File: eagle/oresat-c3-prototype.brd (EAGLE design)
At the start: 99.8 x 94.7 mm, 98 parts, among them J1 J-SAMTEC-TFM-110-X1-XXX-D-RA, J2 U.FL, J3 U.FL, J4 U.FL, J6 J-SAMTEC-TFM-120-X1-XXX-D-RA, J7 FTSH-105-XX-X-DV-K, J8 SD_CARD_SOCKET, Q1 MOSFET-PCH-SOT23-6, Q3 MOSFET-PCH-SOT23-6, Q4 MOSFET-PCH-SOT23-6, Q5 PMV45EN, Q6 PMV45EN, U2 TCAN330, U3 TCAN330, U4 MAX4211CETE, U5 TPS62111RSA, U6 MAX6373KA+21-0078H-L, X1 16MHZ-2.5x2mm

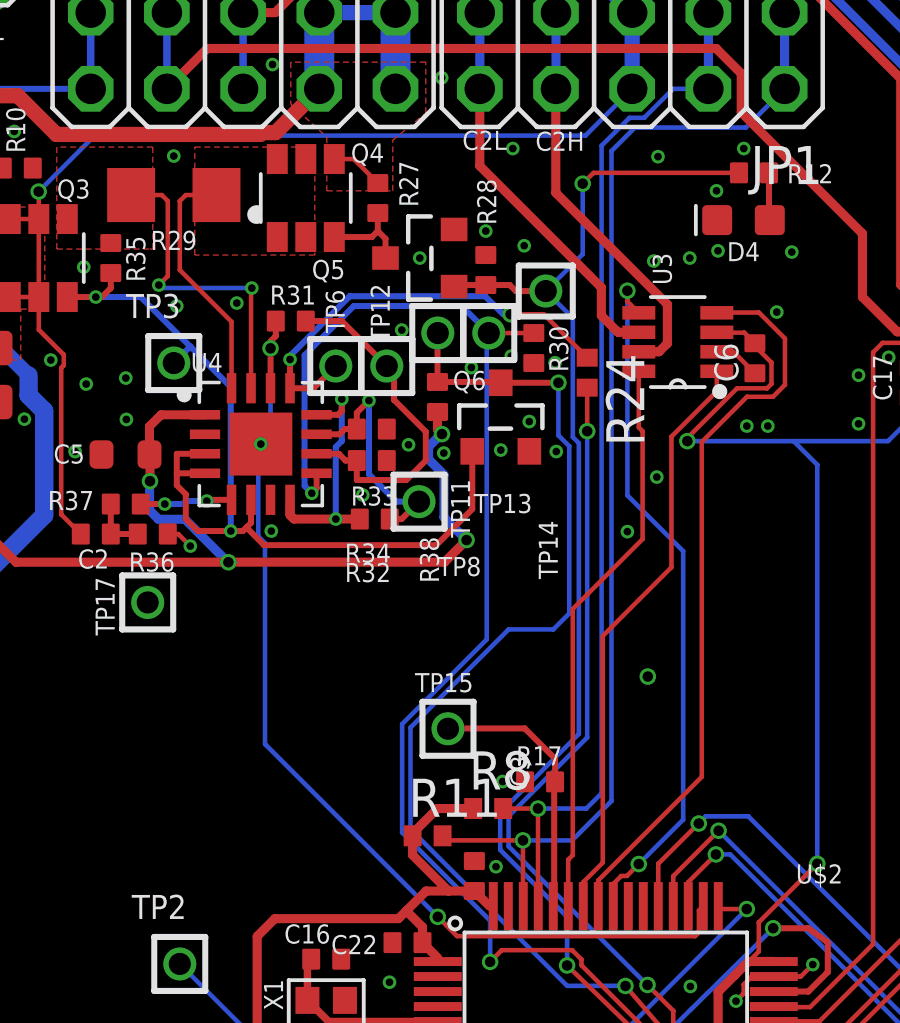
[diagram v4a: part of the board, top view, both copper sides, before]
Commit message: Fixed a couple other error check items
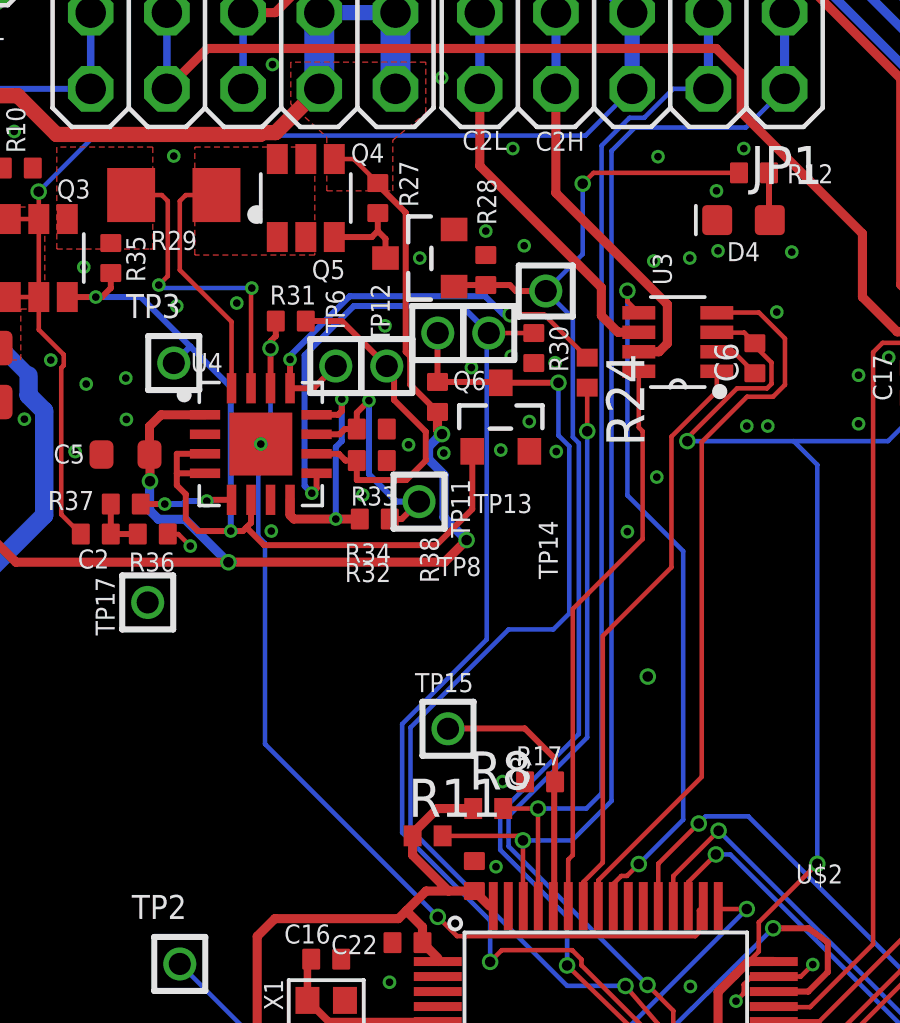
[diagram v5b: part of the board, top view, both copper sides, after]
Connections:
- removed net N$385: Q4.4, R27.2
- net 3.3V: now also Q4.4, R27.2
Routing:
- net 3.3V: track 214.9 -> 225.2 mm
- net N$385: track 1.78 -> 0.00 mm
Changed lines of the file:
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@@
 <wire x1="37.78" y1="43.28" x2="37.78" y2="45.72" width="0.1524" layer="1"/>
 <wire x1="37.525" y1="43.025" x2="37.78" y2="43.28" width="0.1524" layer="1"/>
+<contactref element="R27" pad="2"/>
+<contactref element="Q4" pad="4"/>
+<wire x1="46.4" y1="75.6" x2="45.6" y2="76.4" width="0.1524" layer="1"/>
+<wire x1="45.6" y1="76.4" x2="44.95" y2="76.4" width="0.1524" layer="1"/>
+<wire x1="47.48105" y1="69.823525" x2="47.3301" y2="69.974475" width="0.2032" layer="1"/>
+<wire x1="48.39" y1="67.97" x2="47.48105" y2="68.87895" width="0.2032" layer="1"/>
+<wire x1="46.4" y1="75.5434125" x2="46.4" y2="75.6" width="0.2032" layer="1"/>
+<wire x1="47.48105" y1="68.87895" x2="47.48105" y2="69.823525" width="0.2032" layer="1"/>
+<wire x1="47.3301" y1="69.974475" x2="47.3301" y2="74.6133125" width="0.2032" layer="1"/>
+<wire x1="47.3301" y1="74.6133125" x2="46.4" y2="75.5434125" width="0.2032" layer="1"/>
 </signal>
 <signal name="SDAOPT2">
@@
 <via x="50" y="74" extent="1-16" drill="0.254"/>
 <via x="52.31" y="69.61" extent="1-16" drill="0.254"/>
-<via x="47.2" y="70.7" extent="1-16" drill="0.254"/>
+<via x="46.64" y="70.84" extent="1-16" drill="0.254"/>
 <via x="34.28" y="77.32" extent="1-16" drill="0.254"/>
 <wire x1="31.575" y1="69.125" x2="32.275" y2="69.125" width="0.3" layer="1"/>
@@
 <contactref element="U$3" pad="1"/>
 <contactref element="U$3" pad="THERMAL"/>
-<contactref element="C1" pad="1"/>
 <contactref element="R9" pad="1"/>
 <contactref element="R6" pad="1"/>
@@
 <contactref element="JP2" pad="9"/>
 <via x="55.4" y="59.15" extent="1-16" drill="0.35"/>
+<contactref element="C1" pad="1"/>
 </signal>
 <signal name="PA5/SPI1_SCK">
@@
 <wire x1="55.615" y1="85.625" x2="59.96" y2="81.28" width="0.3048" layer="16"/>
 <wire x1="59.96" y1="81.28" x2="59.96" y2="78.74" width="0.3048" layer="16"/>
-<contactref element="R11" pad="2"/>
-<wire x1="51.239025" y1="53.689025" x2="48.710975" y2="53.689025" width="0.1524" layer="1"/>
-<wire x1="48.710975" y1="53.689025" x2="48.56" y2="53.84" width="0.1524" layer="1"/>
 <wire x1="54.97" y1="77.45" x2="58.67" y2="77.45" width="0.1524" layer="16"/>
 <wire x1="58.67" y1="77.45" x2="59.96" y2="78.74" width="0.1524" layer="16"/>
 <wire x1="54.1902" y1="76.67" x2="54.97" y2="77.4498" width="0.1524" layer="16"/>
 <wire x1="54.97" y1="77.4498" x2="54.97" y2="77.45" width="0.1524" layer="16"/>
+<contactref element="R11" pad="2"/>
+<wire x1="51.239025" y1="53.689025" x2="51.089025" y2="53.839025" width="0.1524" layer="1"/>
+<wire x1="51.089025" y1="53.839025" x2="48.560975" y2="53.839025" width="0.1524" layer="1"/>
+<wire x1="48.560975" y1="53.839025" x2="48.56" y2="53.84" width="0.1524" layer="1"/>
 </signal>
 <signal name="SPARE1">
@@
 <vertex x="46.2" y="84.6"/>
 </polygon>
-<contactref element="R5" pad="2"/>
-<contactref element="C1" pad="2"/>
-<contactref element="U$3" pad="4"/>
 <wire x1="46.99" y1="81.28" x2="46.73" y2="81.54" width="0.508" layer="16"/>
 <wire x1="46.73" y1="88.624" x2="46.73" y2="81.54" width="0.508" layer="16"/>
@@
 <wire x1="42.991" y1="77.281" x2="42.5421875" y2="77.281" width="0.508" layer="1"/>
 <wire x1="42.5421875" y1="77.281" x2="42.4811875" y2="77.22" width="0.508" layer="1"/>
-<wire x1="34.400003125" y1="78.509996875" x2="25.00174375" y2="78.509996875" width="0.508" layer="1"/>
 <wire x1="42.4811875" y1="77.22" x2="35.69" y2="77.22" width="0.508" layer="1"/>
 <wire x1="35.69" y1="77.22" x2="34.400003125" y2="78.509996875" width="0.508" layer="1"/>
+<contactref element="R5" pad="2"/>
+<contactref element="C1" pad="2"/>
+<contactref element="U$3" pad="4"/>
 <wire x1="25.00174375" y1="78.509996875" x2="22.309996875" y2="78.509996875" width="0.508" layer="1"/>
 <wire x1="22.309996875" y1="78.509996875" x2="22.06" y2="78.26" width="0.508" layer="1"/>
 <wire x1="19.255" y1="78.235" x2="22.035" y2="78.235" width="0.5" layer="1"/>
 <wire x1="22.035" y1="78.235" x2="22.06" y2="78.26" width="0.5" layer="1"/>
+<wire x1="34.400003125" y1="78.509996875" x2="25.00174375" y2="78.509996875" width="0.508" layer="1"/>
 </signal>
 <signal name="SDAOPT5">
@@
 <wire x1="54.345" y1="84.355" x2="57.42" y2="81.28" width="0.3048" layer="16"/>
 <wire x1="57.42" y1="81.28" x2="57.42" y2="78.74" width="0.3048" layer="16"/>
-<contactref element="R8" pad="2"/>
-<wire x1="51.74" y1="54.75" x2="50.58" y2="54.75" width="0.1524" layer="1"/>
 <wire x1="54.79" y1="77.7748" x2="55.2798" y2="77.7748" width="0.1524" layer="16"/>
 <wire x1="56.245" y1="78.74" x2="57.42" y2="78.74" width="0.1524" layer="16"/>
@@
 <wire x1="51.74" y1="54.75" x2="53.35106875" y2="54.75" width="0.1524" layer="16"/>
 <wire x1="53.35106875" y1="54.75" x2="53.8608" y2="55.25973125" width="0.1524" layer="16"/>
+<contactref element="R8" pad="2"/>
+<wire x1="51.74" y1="54.75" x2="50.58" y2="54.75" width="0.1524" layer="1"/>
 </signal>
 <signal name="OPD_PWR">
@@
 <wire x1="58.155" y1="86.465" x2="70.3014" y2="74.3186" width="0.3048" layer="16"/>
 </signal>
-<signal name="N$385">
-<contactref element="R27" pad="2"/>
-<contactref element="Q4" pad="4"/>
-<wire x1="46.4" y1="75.6" x2="45.6" y2="76.4" width="0.1524" layer="1"/>
-<wire x1="45.6" y1="76.4" x2="44.95" y2="76.4" width="0.1524" layer="1"/>
-</signal>
 <signal name="N$400">

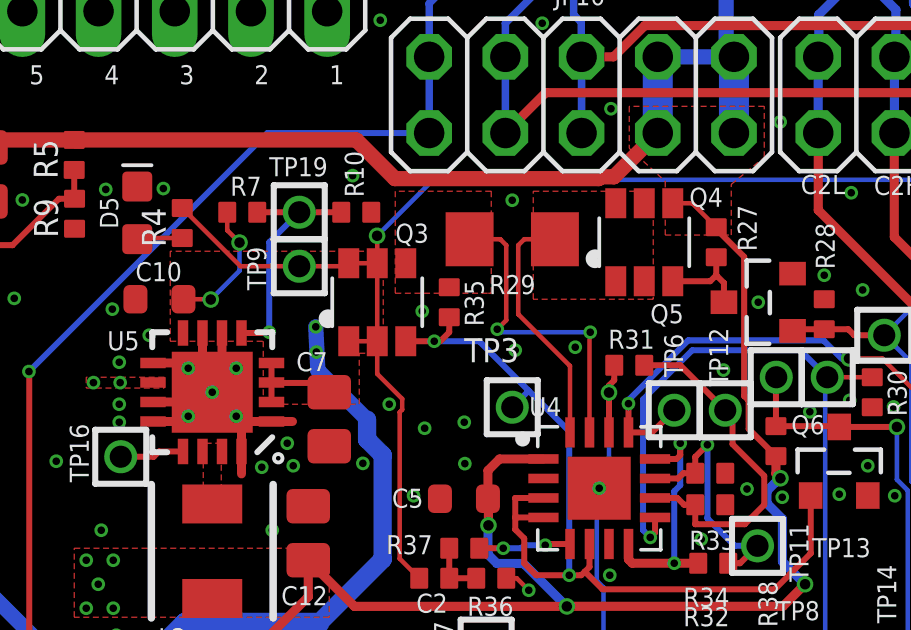
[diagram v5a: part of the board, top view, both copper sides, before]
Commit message: Fixed VBUSP routing around the SPS
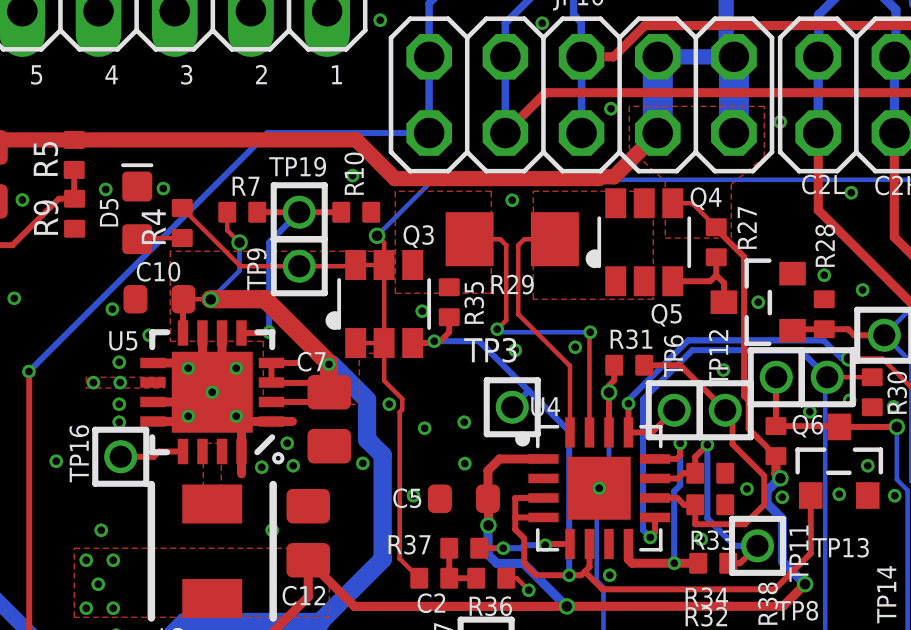
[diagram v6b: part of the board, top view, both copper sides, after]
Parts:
- moved Q3 0.24 mm to (35.3, 73.0)
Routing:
- net VBUSP: track 105.5 -> 112.8 mm, vias 5 -> 4
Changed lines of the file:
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@@
 <attribute name="VALUE" x="32.6" y="64.8" size="0.635" layer="27" font="vector" ratio="20"/>
 </element>
-<element name="Q3" library="Q-MOSFET-PCH-SOT23-6" package="SOT23-6" value="MOSFET-PCH-SOT23-6" x="35.1" y="73.1" smashed="yes">
-<attribute name="MFR" value="Diodes Inc" x="35.1" y="73.1" size="1.778" layer="27" display="off"/>
-<attribute name="MPN" value="DMP3050LVT-7" x="35.1" y="73.1" size="1.778" layer="27" display="off"/>
-<attribute name="NAME" x="35.702" y="75.083" size="0.635" layer="25" font="vector" ratio="20"/>
+<element name="Q3" library="Q-MOSFET-PCH-SOT23-6" package="SOT23-6" value="MOSFET-PCH-SOT23-6" x="35.33" y="73.04" smashed="yes">
+<attribute name="MFR" value="Diodes Inc" x="35.33" y="73.04" size="1.778" layer="27" display="off"/>
+<attribute name="MPN" value="DMP3050LVT-7" x="35.33" y="73.04" size="1.778" layer="27" display="off"/>
+<attribute name="NAME" x="35.932" y="75.023" size="0.635" layer="25" font="vector" ratio="20"/>
 </element>
 <element name="Q4" library="Q-MOSFET-PCH-SOT23-6" package="SOT23-6" value="MOSFET-PCH-SOT23-6" x="44" y="75.1" smashed="yes">
@@
 <vertex x="43.5" y="78.23"/>
 <vertex x="44.7" y="77.13"/>
-<vertex x="44.7" y="75.34"/>
-<vertex x="46.9" y="75.34"/>
+<vertex x="44.7" y="75.24"/>
+<vertex x="46.9" y="75.24"/>
 <vertex x="46.9" y="77.03"/>
 <vertex x="48" y="77.93"/>
@@
 <wire x1="53.075" y1="83.085" x2="54.88" y2="81.28" width="0.508" layer="16"/>
 <wire x1="54.88" y1="81.28" x2="54.88" y2="78.74" width="0.508" layer="16"/>
-<wire x1="35.1" y1="71.8" x2="34.15" y2="71.8" width="0.1524" layer="1"/>
-<wire x1="35.1" y1="74.4" x2="34.15" y2="74.4" width="0.1524" layer="1"/>
-<wire x1="35.1" y1="71.8" x2="35.1" y2="74.4" width="0.1524" layer="1"/>
-<wire x1="34.15" y1="74.4" x2="34.05" y2="74.3" width="0.1524" layer="1"/>
-<wire x1="34.05" y1="74.3" x2="32.5" y2="74.3" width="0.1524" layer="1"/>
+<wire x1="35.33" y1="71.74" x2="34.38" y2="71.74" width="0.1524" layer="1"/>
+<wire x1="35.33" y1="74.34" x2="34.38" y2="74.34" width="0.1524" layer="1"/>
+<wire x1="35.33" y1="71.74" x2="35.33" y2="74.34" width="0.1524" layer="1"/>
+<wire x1="34.38" y1="74.34" x2="34.34" y2="74.3" width="0.1524" layer="1"/>
+<wire x1="34.34" y1="74.3" x2="32.5" y2="74.3" width="0.1524" layer="1"/>
 <wire x1="35.9318" y1="69.8788625" x2="35.9318" y2="69.5211375" width="0.1524" layer="1"/>
 <wire x1="35.9318" y1="69.5211375" x2="35.8482" y2="69.4375375" width="0.1524" layer="1"/>
 <wire x1="35.8482" y1="69.4375375" x2="35.8482" y2="64.5518" width="0.1524" layer="1"/>
 <wire x1="35.8482" y1="64.5518" x2="36.5" y2="63.9" width="0.1524" layer="1"/>
-<wire x1="35.1" y1="71.8" x2="35.1" y2="70.7106625" width="0.1524" layer="1"/>
-<wire x1="35.1" y1="70.7106625" x2="35.9318" y2="69.8788625" width="0.1524" layer="1"/>
+<wire x1="35.33" y1="71.74" x2="35.33" y2="70.4806625" width="0.1524" layer="1"/>
+<wire x1="35.33" y1="70.4806625" x2="35.9318" y2="69.8788625" width="0.1524" layer="1"/>
 <via x="35.09500625" y="75.31500625" extent="1-16" drill="0.35"/>
-<wire x1="35.1" y1="74.4" x2="35.1" y2="75.3100125" width="0.1524" layer="1"/>
-<wire x1="35.1" y1="75.3100125" x2="35.09500625" y2="75.31500625" width="0.1524" layer="1"/>
+<wire x1="35.33" y1="74.34" x2="35.33" y2="75.0800125" width="0.1524" layer="1"/>
+<wire x1="35.33" y1="75.0800125" x2="35.09500625" y2="75.31500625" width="0.1524" layer="1"/>
 <wire x1="53.3218" y1="77.1818" x2="36.9618" y2="77.1818" width="0.1524" layer="16"/>
 <wire x1="35.09500625" y1="75.31500625" x2="36.9618" y2="77.1818" width="0.1524" layer="16"/>
@@
 <wire x1="39.7" y1="66.575" x2="39.7" y2="65.925" width="0.2" layer="1"/>
 <wire x1="39.7" y1="65.925" x2="39.7" y2="65.525" width="0.2" layer="1"/>
-<wire x1="37" y1="71.8" x2="36.05" y2="71.8" width="0.2" layer="1"/>
+<wire x1="37" y1="71.8" x2="36.94" y2="71.74" width="0.2" layer="1"/>
+<wire x1="36.94" y1="71.74" x2="36.28" y2="71.74" width="0.2" layer="1"/>
 <wire x1="37.2" y1="71.8" x2="37" y2="71.8" width="0.2" layer="1"/>
 <via x="37" y="71.8" extent="1-16" drill="0.254"/>
@@
 <wire x1="20.3" y1="28.8" x2="20.3" y2="25.53" width="0.7" layer="16"/>
 <wire x1="20.27" y1="25.5" x2="20.3" y2="25.53" width="0.5" layer="16"/>
-<via x="33.05" y="72.28" extent="1-16" drill="0.254"/>
-<via x="33.07" y="71.44" extent="1-16" drill="0.254"/>
+<via x="33.49" y="71.03" extent="1-16" drill="0.254"/>
 <contactref element="TP20" pad="1"/>
 <wire x1="8.34" y1="78.28" x2="9.4093375" y2="78.28" width="0.1524" layer="16"/>
@@
 <contactref element="U$3" pad="5"/>
 <wire x1="31.575" y1="71.075" x2="31.575" y2="70.425" width="0.2" layer="1"/>
-<wire x1="31.575" y1="70.425" x2="31.575" y2="69.775" width="0.2" layer="1"/>
 <wire x1="31.575" y1="70.425" x2="31.59" y2="70.41" width="0.2" layer="1"/>
 <wire x1="31.59" y1="70.41" x2="33.02" y2="70.41" width="0.2" layer="1"/>
-<wire x1="34.76" y1="69.19" x2="33.12" y2="70.83" width="0.508" layer="16"/>
-<wire x1="33.05" y1="72.28" x2="33.12" y2="70.83" width="0.508" layer="16"/>
 <via x="11.81" y="78.24" extent="1-16" drill="0.254"/>
 <wire x1="11.81" y1="78.24" x2="13.5" y2="78.24" width="0.508" layer="1"/>
@@
 <wire x1="9.4093375" y1="78.28" x2="11.77" y2="78.28" width="0.2" layer="16"/>
 <wire x1="11.77" y1="78.28" x2="11.81" y2="78.24" width="0.2" layer="16"/>
-<wire x1="34.76" y1="68.52395" x2="34.76" y2="69.19" width="0.6096" layer="16"/>
 <wire x1="35.2804" y1="68.00355" x2="34.76" y2="68.52395" width="0.6096" layer="16"/>
 <wire x1="33.15" y1="62.4" x2="35.2804" y2="64.5304" width="0.6096" layer="16"/>
 <wire x1="35.2804" y1="64.5304" x2="35.2804" y2="68.00355" width="0.6096" layer="16"/>
-<wire x1="28.64" y1="73.2" x2="29.54" y2="73.2" width="0.1524" layer="1"/>
+<wire x1="28.64" y1="73.2" x2="28.73" y2="73.2" width="0.1524" layer="1"/>
+<wire x1="28.73" y1="73.2" x2="29.54" y2="73.2" width="0.1524" layer="1"/>
 <wire x1="29.54" y1="73.2" x2="29.55" y2="73.19" width="0.1524" layer="1"/>
 <via x="29.55" y="73.19" extent="1-16" drill="0.35"/>
@@
 <wire x1="30.509271875" y1="75.089271875" x2="30.509271875" y2="74.149271875" width="0.1524" layer="16"/>
 <wire x1="30.509271875" y1="74.149271875" x2="29.55" y2="73.19" width="0.1524" layer="16"/>
+<wire x1="34.76" y1="68.52395" x2="34.76" y2="69.85" width="0.6096" layer="16"/>
+<wire x1="33.49" y1="70.11" x2="33.5" y2="70.1" width="0.6096" layer="1"/>
+<wire x1="31.575" y1="69.775" x2="33.095" y2="69.775" width="0.2" layer="1"/>
+<wire x1="33.095" y1="69.775" x2="33.11" y2="69.76" width="0.2" layer="1"/>
+<wire x1="31.575" y1="71.075" x2="32.385" y2="71.075" width="0.2" layer="1"/>
+<wire x1="32.385" y1="71.075" x2="32.39" y2="71.07" width="0.2" layer="1"/>
+<wire x1="28.625" y1="72.075" x2="28.625" y2="73.095" width="0.2" layer="1"/>
+<wire x1="28.625" y1="73.095" x2="28.73" y2="73.2" width="0.2" layer="1"/>
+<wire x1="29.54" y1="73.2" x2="31.36" y2="73.2" width="0.609" layer="1"/>
+<wire x1="33.49" y1="71.03" x2="33.49" y2="70.11" width="0.609" layer="1"/>
+<wire x1="34.76" y1="69.85" x2="33.58" y2="71.03" width="0.609" layer="16"/>
+<wire x1="33.58" y1="71.03" x2="33.49" y2="71.03" width="0.609" layer="16"/>
+<wire x1="31.36" y1="73.2" x2="33.49" y2="71.07" width="0.609" layer="1"/>
+<wire x1="33.49" y1="71.07" x2="33.49" y2="71.03" width="0.609" layer="1"/>
+<wire x1="33.5" y1="70.1" x2="33.11" y2="69.76" width="0" layer="19" extent="1-1"/>
+<wire x1="33.02" y1="70.41" x2="33.5" y2="70.1" width="0" layer="19" extent="1-1"/>
 </signal>
 <signal name="N$398">
